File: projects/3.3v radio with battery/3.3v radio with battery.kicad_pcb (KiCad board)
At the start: 2 copper layers, 130 x 80 mm, 14 parts, among them J1 USB_B

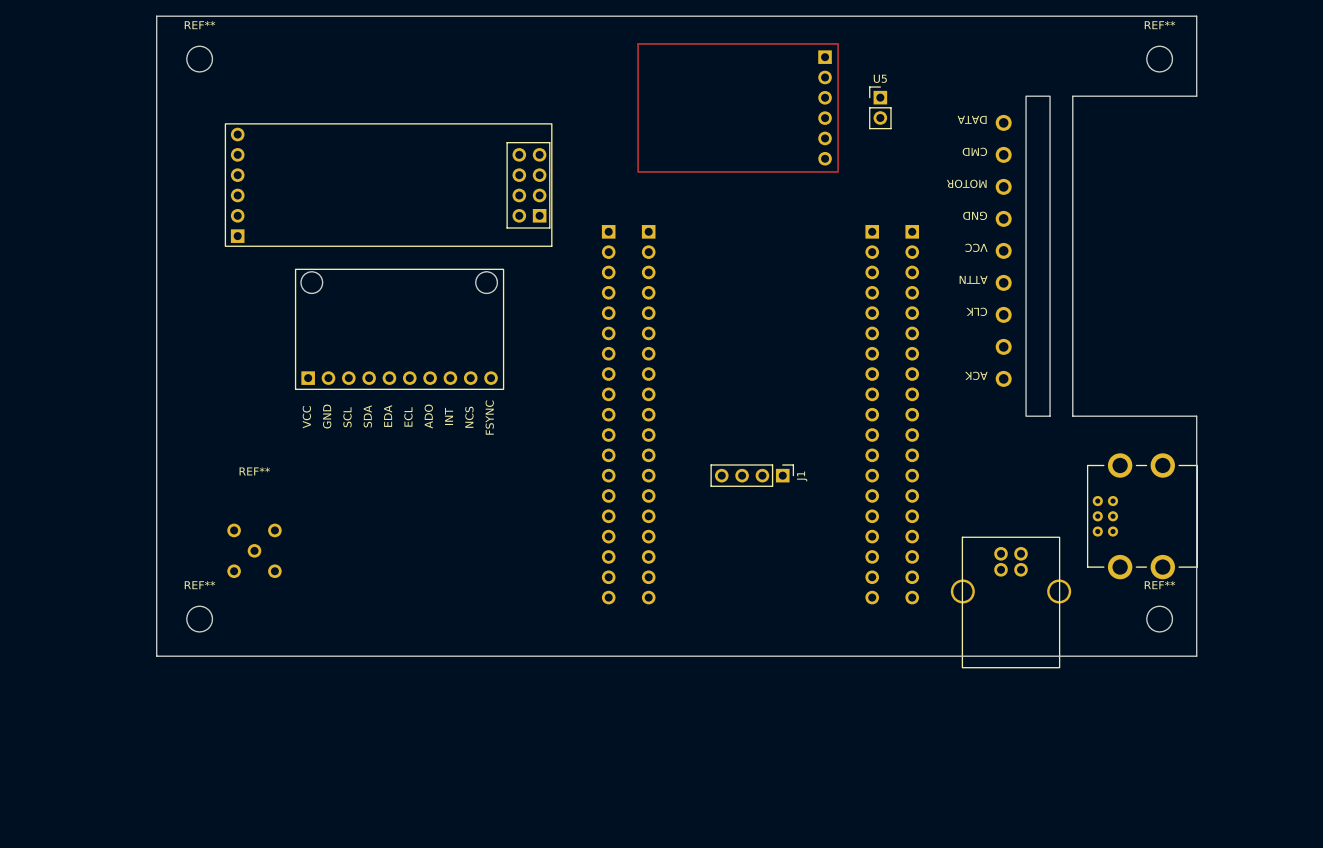
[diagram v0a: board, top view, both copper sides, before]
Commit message: update 3.3v rad
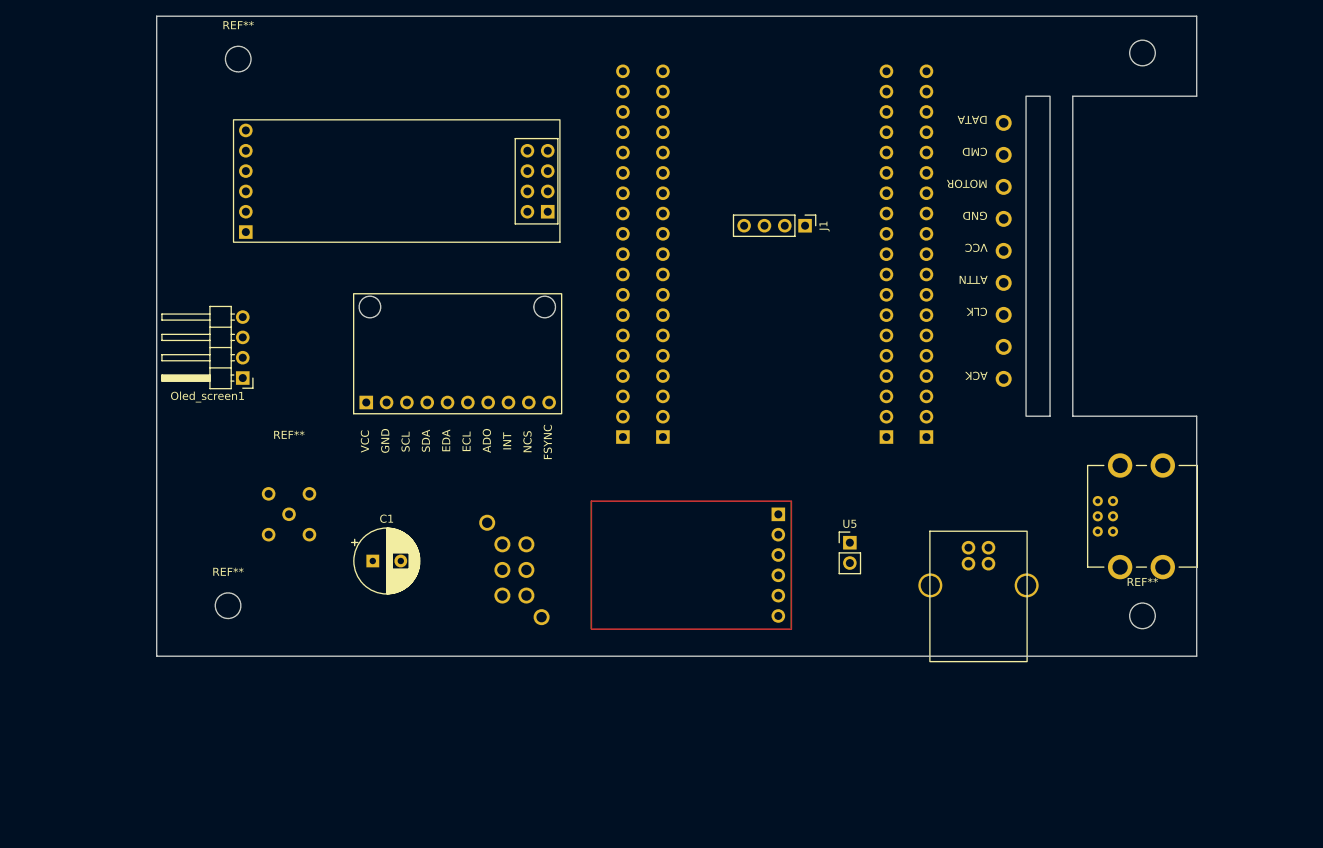
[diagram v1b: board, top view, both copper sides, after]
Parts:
- added C1: CP_Axial_L10.0mm_D4.5mm_P15.00mm, Capacitor_THT:CP_Radial_D8.0mm_P3.50mm, F.Cu at (115.6, 104.9)
- added Oled_screen1: ~, Connector_PinHeader_2.54mm:PinHeader_1x04_P2.54mm_Horizontal, F.Cu at (99.4, 82.0)
- added REF**: Switch A03 PS-22F03, Footprints_cez:Switch A03 PS-22F03, F.Cu at (133.2, 93.3)
- moved U3 57.4 mm to (154.9, 90.9)
- moved U5 55.8 mm to (175.3, 102.6)
- moved J1 31.4 mm to (169.7, 63.0)
- moved MPU1 7.87 mm to (108.7, 79.9)
- moved REF** 6.29 mm to (105.1, 89.7)
- moved REF** 4.83 mm to (98.8, 42.2)
- moved ESP32-WROOM-32U1 4.51 mm to (167.1, 77.2), turned to 180 degrees
- moved U4 4.13 mm to (191.2, 91.9)
- moved REF** 3.93 mm to (97.5, 110.5)
- moved REF** 2.28 mm to (211.8, 41.4)
- moved REF** 2.18 mm to (211.8, 111.8)
- moved NRF1 1.14 mm to (137.5, 61.2)

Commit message: a lot of project updates
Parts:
- removed the REF** at (211.8, 41.4)
- removed the REF** at (211.8, 111.8)
- removed the REF** at (133.2, 93.3)
- removed the REF** at (98.8, 42.2)
- removed the REF** at (97.5, 110.5)
- added C2: CP_Axial_L10.0mm_D4.5mm_P15.00mm, Capacitor_THT:CP_Radial_D8.0mm_P3.50mm, F.Cu at (201.5, 82.7)
- added C3: CP_Axial_L10.0mm_D4.5mm_P15.00mm, Capacitor_THT:CP_Radial_D8.0mm_P3.50mm, F.Cu at (211.5, 82.7)
- added REF**: MountingHole_3.2mm_M3, MountingHole:MountingHole_3.2mm_M3, F.Cu at (222.2, 54.0)
- added REF**: MountingHole_3.2mm_M3, MountingHole:MountingHole_3.2mm_M3, F.Cu at (222.2, 133.5)
- added REF**: MountingHole_3.2mm_M3, MountingHole:MountingHole_3.2mm_M3, F.Cu at (122.2, 54.0)
- added REF**: MountingHole_3.2mm_M3, MountingHole:MountingHole_3.2mm_M3, F.Cu at (122.2, 133.5)
- added SMA ANTENNA: PinHeader_1x01_P2.00mm_Vertical, Connector_PinHeader_2.00mm:PinHeader_1x01_P2.00mm_Vertical, F.Cu at (211.5, 119.1)
- added TP1: TestPoint, Connector_PinHeader_2.54mm:PinHeader_1x01_P2.54mm_Vertical, F.Cu at (144.9, 128.8)
- added U6: ~, Footprints_cez:Switch A03 PS-22F03, F.Cu at (135.3, 116.1)
- U5: footprint Connector_PinHeader_2.54mm:PinHeader_1x02_P2.54mm_Vertical -> Footprints_cez:BH-18650-PC2
- moved REF** 129.1 mm to (230.9, 119.1), turned to -90 degrees
- moved Oled_screen1 118.7 mm to (217.8, 89.9), turned to 0 degrees
- moved U1 112.6 mm to (105.9, 61.2), turned to 90 degrees
- moved MPU1 111.5 mm to (209.5, 127.4), turned to -90 degrees
- moved C1 79.1 mm to (191.5, 82.7), turned to -90 degrees
- moved U4 75.1 mm to (124.3, 126.1), turned to -90 degrees
- moved J1 69.1 mm to (127.3, 117.6)
- moved U2 66.0 mm to (127.7, 91.1), turned to 0 degrees
- moved NRF1 48.0 mm to (185.3, 64.5), turned to 0 degrees
- moved U5 31.1 mm to (144.9, 96.1)
- moved U3 24.3 mm to (161.7, 114.3)
- moved ESP32-WROOM-32U1 20.7 mm to (147.1, 72.1), turned to 90 degrees
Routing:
- net Net-(MPU1-GND): track 0.00 -> 278.3 mm
- net Net-(ESP32-WROOM-32U1-3.3v): track 0.00 -> 226.3 mm
- net Net-(ESP32-WROOM-32U1-SCL/22): track 0.00 -> 184.0 mm
- net Net-(ESP32-WROOM-32U1-SDA/21): track 0.00 -> 178.3 mm
- net Net-(ESP32-WROOM-32U1-MOSI/23): track 0.00 -> 119.8 mm
- net Net-(ESP32-WROOM-32U1-MISO/19): track 0.00 -> 109.7 mm
- net Net-(J1-GND): track 0.00 -> 96.6 mm
- net Net-(ESP32-WROOM-32U1-SCK/18): track 0.00 -> 86.2 mm
- net Net-(U3-GND_IN): track 0.00 -> 71.2 mm
- net Net-(U3-VIN): track 0.00 -> 63.8 mm
- net Net-(U3-BAT_GND): track 0.00 -> 54.9 mm
- net Net-(ESP32-WROOM-32U1-SS/5): track 0.00 -> 53.3 mm
- net Net-(J1-VBUS): track 0.00 -> 47.9 mm
- net Net-(U3-BAT_POSITIVE): track 0.00 -> 44.4 mm
- net Net-(ESP32-WROOM-32U1-17): track 0.00 -> 37.8 mm
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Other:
- board size 130 x 80 mm -> 130 x 90 mm
- board text added: "CRJ"
- board text added: "GND D+ D- VCC"

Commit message: only multi remote left
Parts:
- added GPS1: ~, Footprints_cez:GY-NEO6MV2_flipped, F.Cu at (102.2, 72.3)
- added U7: ~, Footprints_cez:BME280, F.Cu at (115.1, 119.7)
- moved J1 27.7 mm to (99.6, 118.1)
- moved U1 27.7 mm to (78.2, 61.2)
- moved U2 27.7 mm to (100.0, 91.1)
- moved U4 27.7 mm to (96.6, 126.1)
- moved REF** 26.2 mm to (96.5, 58.7)
- moved REF** 26.2 mm to (96.5, 128.7)
- moved U6 25.4 mm to (109.9, 115.2)
- moved TP1 23.4 mm to (121.5, 127.9)
- moved U3 17.0 mm to (144.8, 112.8)
- moved MPU1 9.61 mm to (199.9, 126.9)
- moved U5 0.76 mm to (144.1, 96.1)
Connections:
- C1 pad 2: Net-(MPU1-GND) -> Net-(GPS1-GND)
- C2 pad 2: Net-(MPU1-GND) -> Net-(GPS1-GND)
- C3 pad 2: Net-(MPU1-GND) -> Net-(GPS1-GND)
- ESP32-WROOM-32U1 pad 14: unconnected-(ESP32-WROOM-32U1-GND-Pad14) -> Net-(GPS1-GND)
- ESP32-WROOM-32U1 pad 20: Net-(MPU1-GND) -> unconnected-(ESP32-WROOM-32U1-GND-Pad20)
- ESP32-WROOM-32U1 pad 30: Net-(ESP32-WROOM-32U1-17) -> Net-(ESP32-WROOM-32U1-TX2/17)
- ESP32-WROOM-32U1 pad 31: Net-(ESP32-WROOM-32U1-16) -> Net-(ESP32-WROOM-32U1-RX2/16)
- ESP32-WROOM-32U1 pad 7: unconnected-(ESP32-WROOM-32U1-32-Pad7) -> Net-(ESP32-WROOM-32U1-32)
- ESP32-WROOM-32U1 pad 8: unconnected-(ESP32-WROOM-32U1-33-Pad8) -> Net-(ESP32-WROOM-32U1-33)
- MPU1 pad 2: Net-(MPU1-GND) -> Net-(GPS1-GND)
- NRF1 pad 1: Net-(MPU1-GND) -> Net-(GPS1-GND)
- NRF1 pad 3: Net-(ESP32-WROOM-32U1-16) -> Net-(ESP32-WROOM-32U1-32)
- NRF1 pad 4: Net-(ESP32-WROOM-32U1-17) -> Net-(ESP32-WROOM-32U1-33)
- Oled_screen1 pad 2: Net-(MPU1-GND) -> Net-(GPS1-GND)
- U1 pad 6: Net-(MPU1-GND) -> Net-(GPS1-GND)
- U2 pad 4: Net-(MPU1-GND) -> Net-(GPS1-GND)
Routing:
- net Net-(GPS1-GND): track 0.00 -> 296.7 mm
- net Net-(MPU1-GND): track 278.3 -> 0.00 mm
- net Net-(ESP32-WROOM-32U1-SCL/22): track 184.0 -> 305.3 mm
- net Net-(ESP32-WROOM-32U1-SDA/21): track 178.3 -> 295.6 mm
- net Net-(ESP32-WROOM-32U1-TX2/17): track 0.00 -> 62.8 mm
- net Net-(ESP32-WROOM-32U1-RX2/16): track 0.00 -> 62.8 mm
- net Net-(ESP32-WROOM-32U1-3.3v): track 226.3 -> 280.4 mm
- net Net-(ESP32-WROOM-32U1-33): track 0.00 -> 47.6 mm
- net Net-(ESP32-WROOM-32U1-32): track 0.00 -> 47.6 mm
- net Net-(ESP32-WROOM-32U1-17): track 37.8 -> 0.00 mm
- net Net-(ESP32-WROOM-32U1-16): track 31.7 -> 0.00 mm
- net Net-(J1-GND): track 96.6 -> 66.5 mm
- net Net-(ESP32-WROOM-32U1-SS/5): track 53.3 -> 83.1 mm
- net Net-(ESP32-WROOM-32U1-SCK/18): track 86.2 -> 115.2 mm
- net Net-(ESP32-WROOM-32U1-MISO/19): track 109.7 -> 129.6 mm
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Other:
- board size 130 x 90 mm -> 157.7 x 90 mm
- board text added: "+"

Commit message: and to the factory it goes
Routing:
- net Net-(ESP32-WROOM-32U1-3.3v): track 280.4 -> 282.5 mm
- net Net-(GPS1-GND): track 296.7 -> 298.3 mm
- net Net-(ESP32-WROOM-32U1-SCL/22): track 305.3 -> 306.2 mm
